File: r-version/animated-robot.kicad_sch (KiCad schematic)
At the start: 81 parts, among them J1 USB_C_Receptacle_USB2.0_16P, J2 Conn_02x03_Odd_Even, J3 Conn_01x02, J4 Conn_01x05, Q1 Q_NMOS_GDS, Q2 Q_NMOS_GDS, Q3 Q_NMOS_GDS, Q4 Q_NMOS_GDS, Q5 Q_NMOS_GDS, Q6 Q_NMOS_GDS, U1 LKS32MC034DOFxQx, U3 XL1509-ADJ, Y1 Crystal_GND24_Small

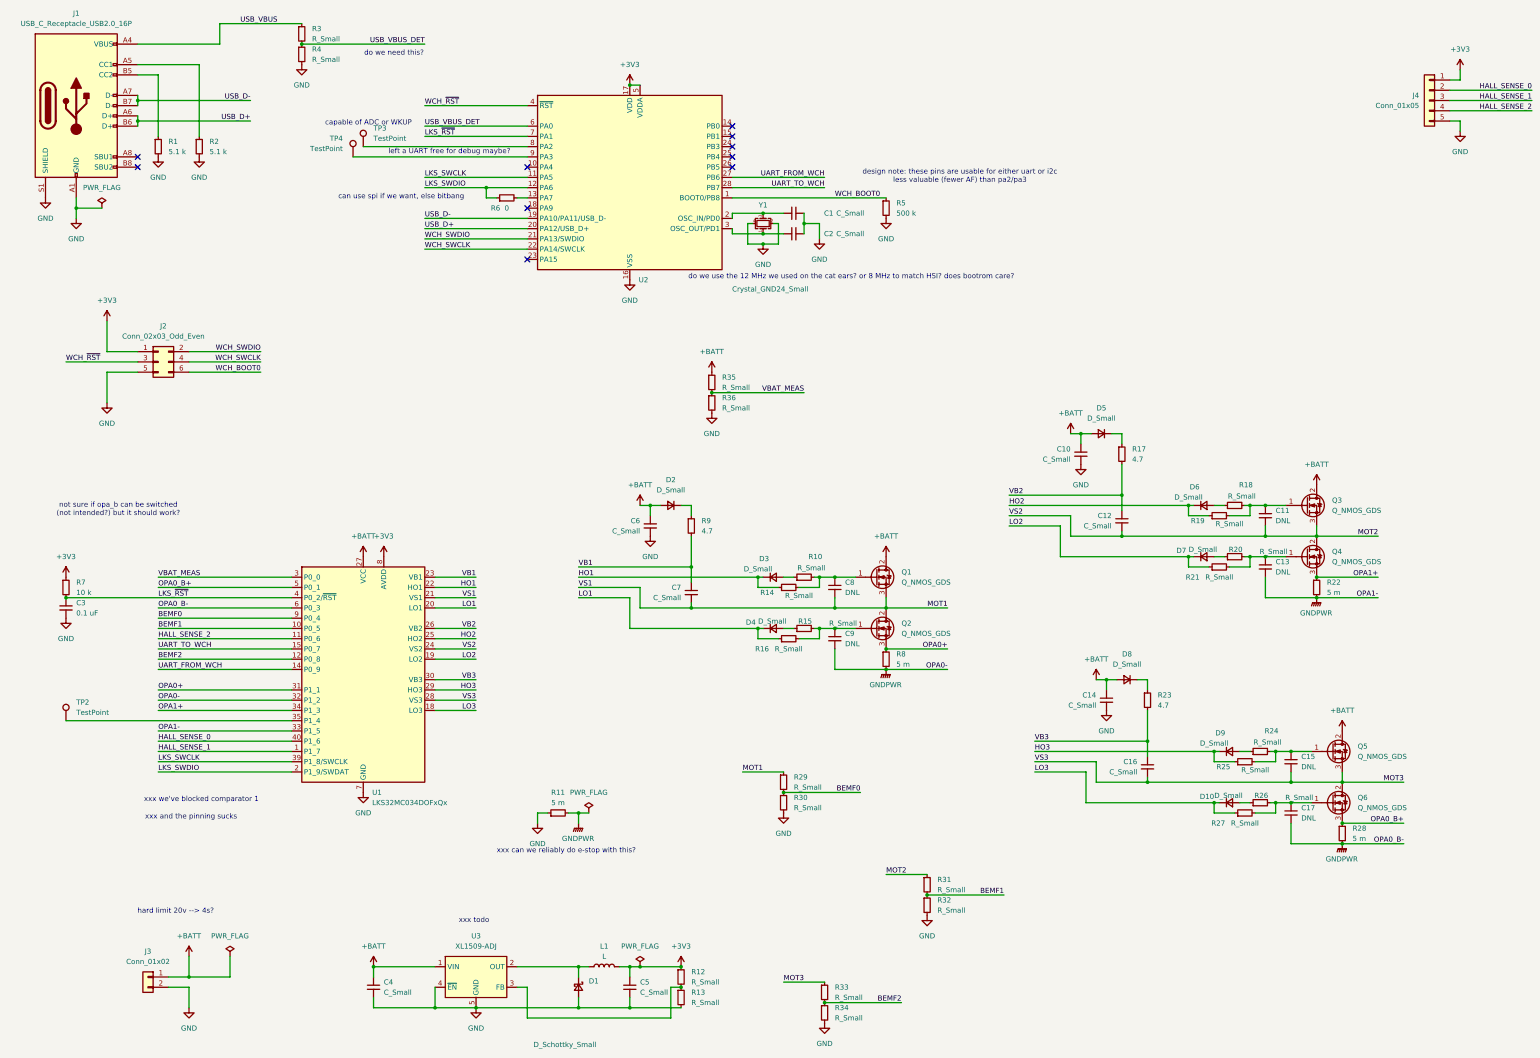
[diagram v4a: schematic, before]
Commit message: fixes to pin assignment
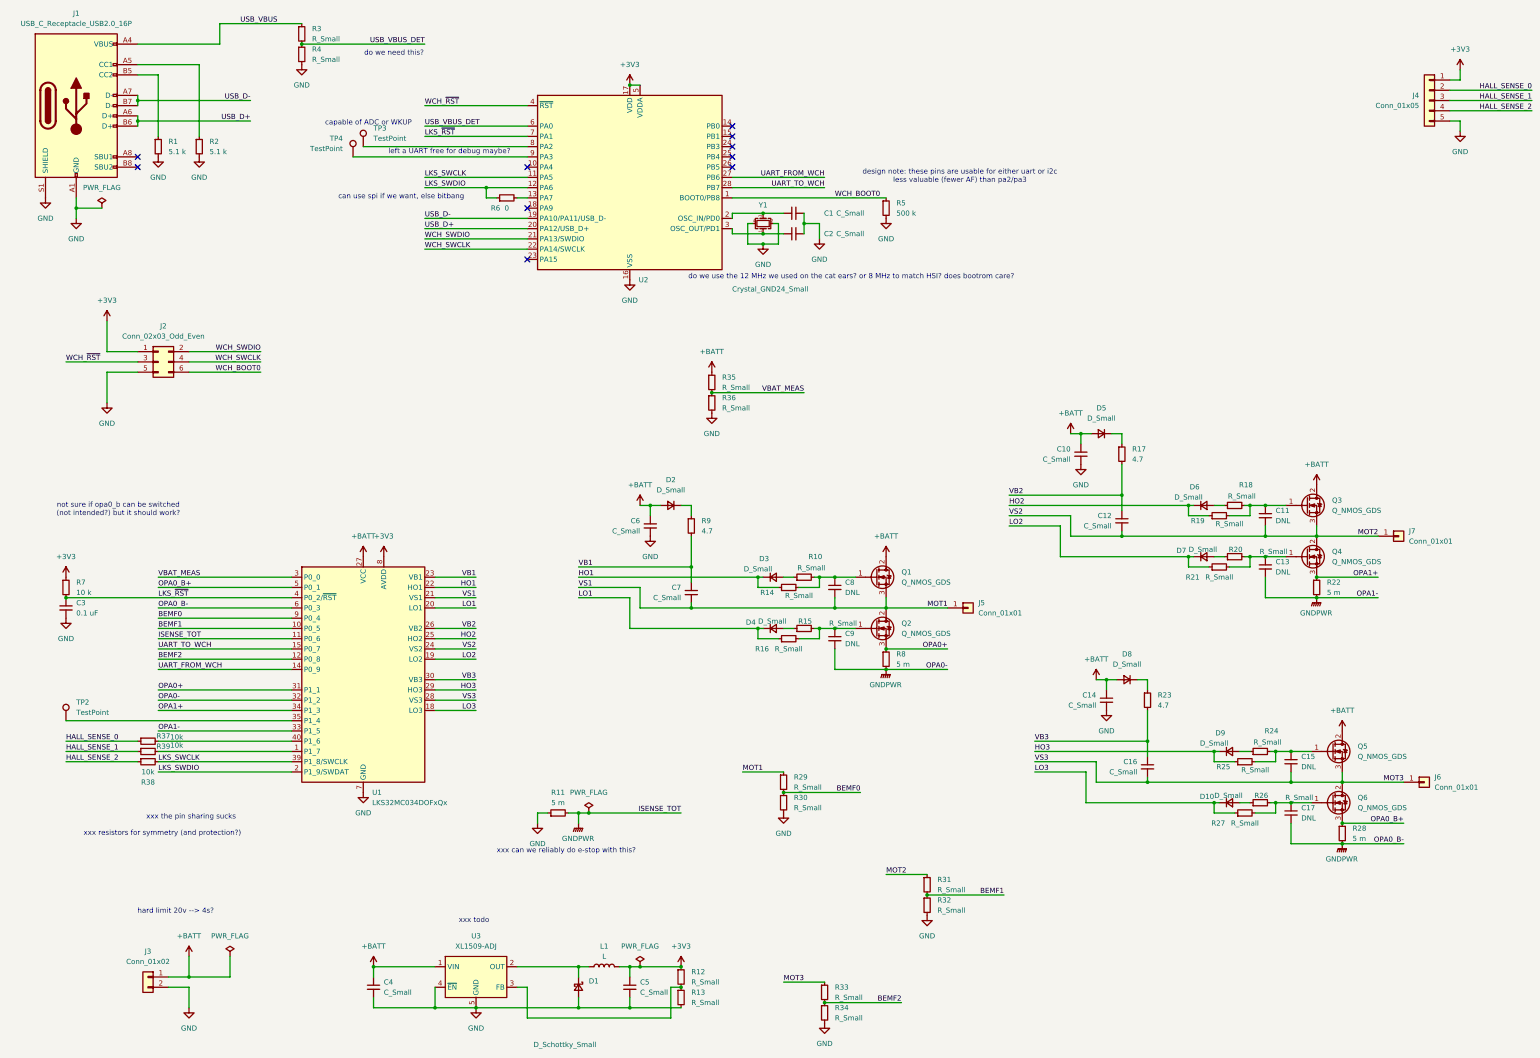
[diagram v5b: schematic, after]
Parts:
- added J5, J6, J7: Conn_01x01, symbol Connector_Generic:Conn_01x01
- added R37, R38, R39: 10k, symbol Device:R_Small
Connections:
- net GNDPWR: now also U1.11 (P0_6)
- net HALL_SENSE_0: now also R37.1; no longer U1.40 (P1_6)
- net HALL_SENSE_1: now also R39.1; no longer U1.1 (P1_7)
- net HALL_SENSE_2: now also R38.1; no longer U1.11 (P0_6)
- net LKS_SWCLK: now also R38.2
- net MOT1: now also J5.1 (Pin_1)
- net MOT2: now also J7.1 (Pin_1)
- net MOT3: now also J6.1 (Pin_1)
- new net: R39.2, U1.1 (P1_7)
- new net: R37.2, U1.40 (P1_6)
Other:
- note added: "not sure if opa0_b can be switched (not intended?) but it should work?"
- note added: "xxx resistors for symmetry (and protection?)"
- note added: "xxx the pin sharing sucks"
- note removed: "not sure if opa_b can be switched (not intended?) but it should work?"
- note removed: "xxx and the pinning sucks"
- note removed: "xxx we've blocked comparator 1"

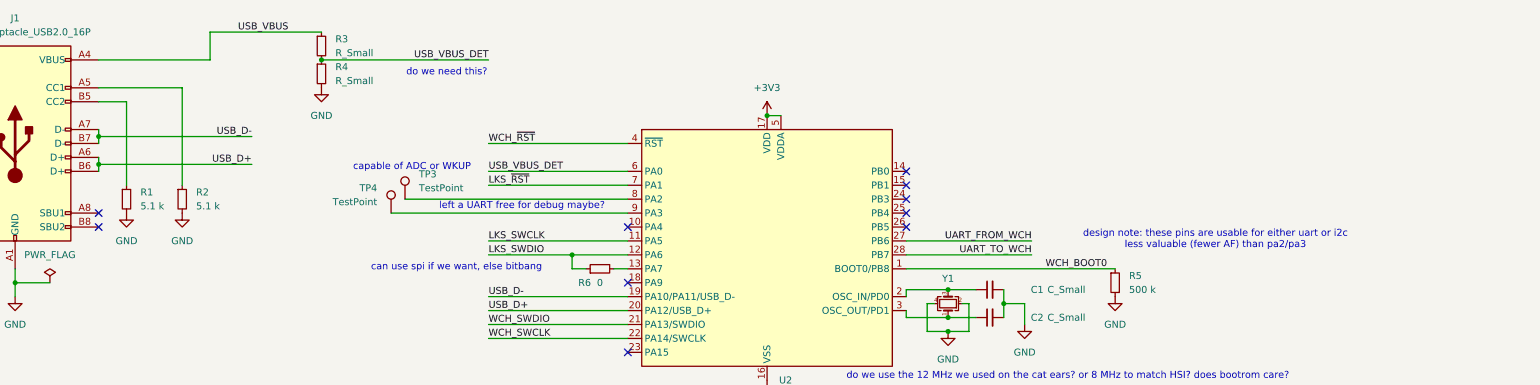
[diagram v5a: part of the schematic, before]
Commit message: fix wch usb vbus det
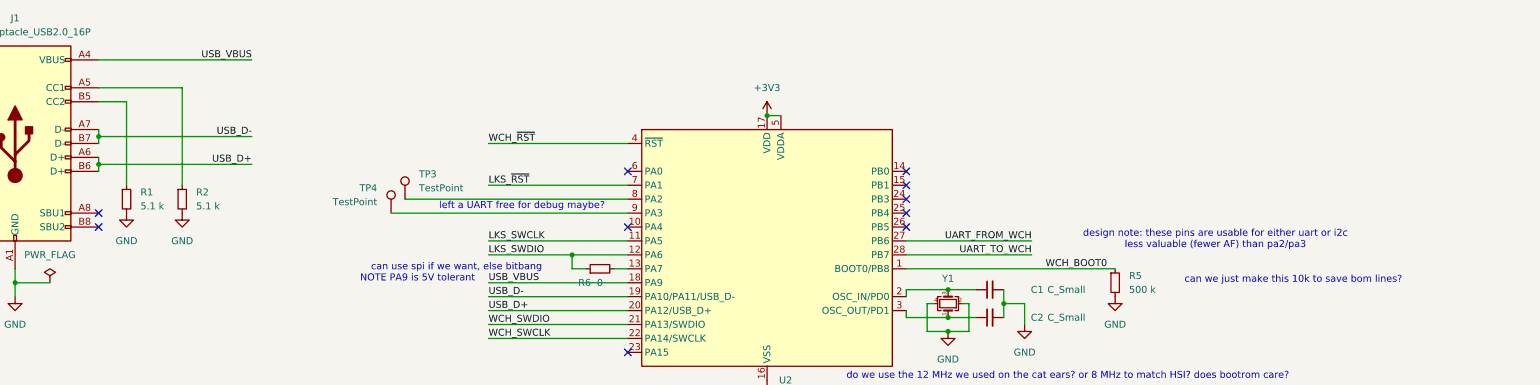
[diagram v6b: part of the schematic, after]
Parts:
- removed R3, R4: R_Small, symbol Device:R_Small
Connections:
- net USB_VBUS: now also U2.18 (PA9)
- net USB_VBUS_DET: no longer names the net of U2.6 (PA0)
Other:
- note added: "NOTE PA9 is 5V tolerant"
- note added: "can we just make this 10k to save bom lines?"
- note removed: "capable of ADC or WKUP"
- note removed: "do we need this?"

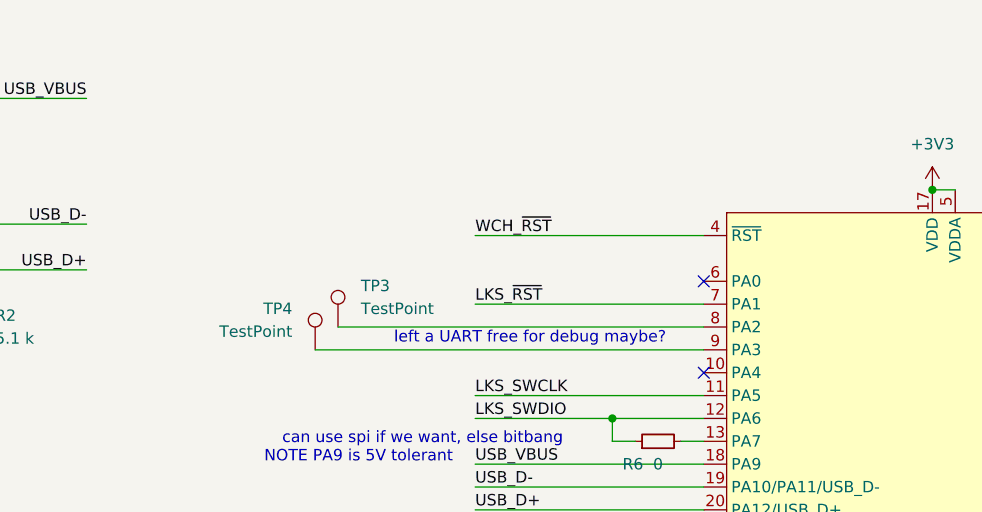
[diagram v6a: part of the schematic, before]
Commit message: add capacitor on wch reset
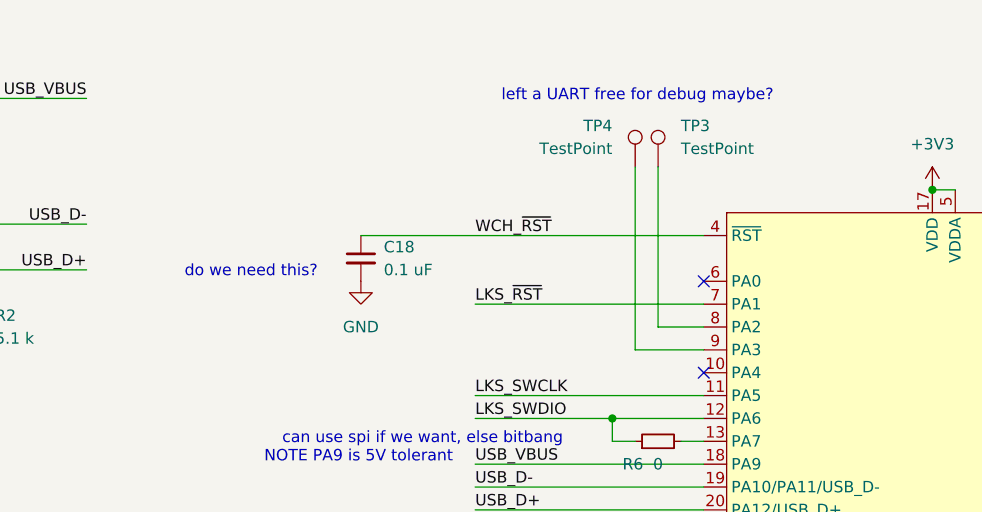
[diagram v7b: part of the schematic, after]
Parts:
- added C18: 0.1 uF, symbol Device:C_Small
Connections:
- net GND: now also C18.2
- net WCH_~{RST}: now also C18.1
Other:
- note added: "do we need this?"
- moved on the sheet: TP3, TP4
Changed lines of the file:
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@@
 	(wire
 		(pts
-			(xy 96.52 50.8) (xy 139.7 50.8)
-		)
-		(stroke
-			(width 0)
-			(type default)
-		)
-	)
-	(wire
-		(pts
 			(xy 180.34 162.56) (xy 215.9 162.56)
 		)
@@
 	(wire
 		(pts
+			(xy 132.08 30.48) (xy 132.08 50.8)
+		)
+		(stroke
+			(width 0)
+			(type default)
+		)
+	)
+	(wire
+		(pts
 			(xy 25.4 160.02) (xy 81.28 160.02)
 		)
@@
 	(wire
 		(pts
-			(xy 114.3 38.1) (xy 139.7 38.1)
-		)
-		(stroke
-			(width 0)
-			(type default)
-		)
-	)
-	(wire
-		(pts
 			(xy 325.12 210.82) (xy 328.93 210.82)
 		)
@@
 	(wire
 		(pts
-			(xy 99.06 48.26) (xy 139.7 48.26)
-		)
-		(stroke
-			(width 0)
-			(type default)
-		)
-	)
-	(wire
-		(pts
 			(xy 132.08 60.96) (xy 129.54 60.96)
 		)
@@
 	(wire
 		(pts
+			(xy 134.62 48.26) (xy 139.7 48.26)
+		)
+		(stroke
+			(width 0)
+			(type default)
+		)
+	)
+	(wire
+		(pts
 			(xy 322.58 144.78) (xy 335.28 144.78)
 		)
@@
 	(wire
 		(pts
+			(xy 134.62 30.48) (xy 134.62 48.26)
+		)
+		(stroke
+			(width 0)
+			(type default)
+		)
+	)
+	(wire
+		(pts
 			(xy 215.9 154.94) (xy 220.98 154.94)
 		)
@@
 	(wire
 		(pts
+			(xy 132.08 50.8) (xy 139.7 50.8)
+		)
+		(stroke
+			(width 0)
+			(type default)
+		)
+	)
+	(wire
+		(pts
 			(xy 27.94 63.5) (xy 27.94 60.96)
 		)
@@
 	(wire
 		(pts
+			(xy 101.6 38.1) (xy 139.7 38.1)
+		)
+		(stroke
+			(width 0)
+			(type default)
+		)
+	)
+	(wire
+		(pts
 			(xy 207.01 170.18) (xy 212.09 170.18)
 		)
@@
 	(text "left a UART free for debug maybe?"
 		(exclude_from_sim no)
-		(at 120.396 49.53 0)
+		(at 132.334 22.606 0)
 		(effects
 			(font
@@
 		)
 	)
+	(text "do we need this?"
+		(exclude_from_sim no)
+		(at 89.408 42.164 0)
+		(effects
+			(font
+				(size 1.27 1.27)
+			)
+		)
+	)
 	(text "hard limit 20v --> 4s?"
 		(exclude_from_sim no)
@@
 	(symbol
 		(lib_id "Connector:TestPoint")
-		(at 99.06 48.26 0)
+		(at 134.62 30.48 0)
 		(unit 1)
 		(exclude_from_sim no)
@@
 		(fields_autoplaced yes)
 		(property "Reference" "TP3"
-			(at 101.6 43.6879 0)
+			(at 137.16 25.9079 0)
 			(effects
 				(font
@@
 		)
 		(property "Value" "TestPoint"
-			(at 101.6 46.2279 0)
+			(at 137.16 28.4479 0)
 			(effects
 				(font
@@
 		)
 		(property "Footprint" ""
-			(at 104.14 48.26 0)
+			(at 139.7 30.48 0)
 			(effects
 				(font
@@
 		)
 		(property "Datasheet" "~"
-			(at 104.14 48.26 0)
+			(at 139.7 30.48 0)
 			(effects
 				(font
@@
 		)
 		(property "Description" "test point"
-			(at 99.06 48.26 0)
+			(at 134.62 30.48 0)
 			(effects
 				(font
@@
 	(symbol
 		(lib_id "Connector:TestPoint")
-		(at 96.52 50.8 0)
+		(at 132.08 30.48 0)
 		(mirror y)
 		(unit 1)
@@
 		(dnp no)
 		(property "Reference" "TP4"
-			(at 93.98 46.2279 0)
+			(at 129.54 25.9079 0)
 			(effects
 				(font
@@
 		)
 		(property "Value" "TestPoint"
-			(at 93.98 48.7679 0)
+			(at 129.54 28.4479 0)
 			(effects
 				(font
@@
 		)
 		(property "Footprint" ""
-			(at 91.44 50.8 0)
+			(at 127 30.48 0)
 			(effects
 				(font
@@
 		)
 		(property "Datasheet" "~"
-			(at 91.44 50.8 0)
+			(at 127 30.48 0)
 			(effects
 				(font
@@
 		)
 		(property "Description" "test point"
-			(at 96.52 50.8 0)
+			(at 132.08 30.48 0)
 			(effects
 				(font
@@
 	)
 	(symbol
+		(lib_id "power:GND")
+		(at 101.6 43.18 0)
+		(unit 1)
+		(exclude_from_sim no)
+		(in_bom yes)
+		(on_board yes)
+		(dnp no)
+		(fields_autoplaced yes)
+		(property "Reference" "#PWR05"
+			(at 101.6 49.53 0)
+			(effects
+				(font
+					(size 1.27 1.27)
+				)
+				(hide yes)
+			)
+		)
+		(property "Value" "GND"
+			(at 101.6 48.26 0)
+			(effects
+				(font
+					(size 1.27 1.27)
+				)
+			)
+		)
+		(property "Footprint" ""
+			(at 101.6 43.18 0)
+			(effects
+				(font
+					(size 1.27 1.27)
+				)
+				(hide yes)
+			)
+		)
+		(property "Datasheet" ""
+			(at 101.6 43.18 0)
+			(effects
+				(font
+					(size 1.27 1.27)
+				)
+				(hide yes)
+			)
+		)
+		(property "Description" "Power symbol creates a global label with name \"GND\" , ground"
+			(at 101.6 43.18 0)
+			(effects
+				(font
+					(size 1.27 1.27)
+				)
+				(hide yes)
+			)
+		)
+		(pin "1"
+		)
+		(instances
+			(project "animated-robot"
+				(path "/8ca1d24f-691f-408a-ac85-5b754cca902e"
+					(reference "#PWR05")
+					(unit 1)
+				)
+			)
+		)
+	)
+	(symbol
 		(lib_id "power:GNDPWR")
 		(at 152.4 215.9 0)
@@
 					(unit 1)
 				)
+			)
+		)
+	)
+	(symbol
+		(lib_id "Device:C_Small")
+		(at 101.6 40.64 0)
+		(unit 1)
+		(exclude_from_sim no)
+		(in_bom yes)
+		(on_board yes)
+		(dnp no)
+		(fields_autoplaced yes)
+		(property "Reference" "C18"
+			(at 104.14 39.3762 0)
+			(effects
+				(font
+					(size 1.27 1.27)
+				)
+				(justify left)
+			)
+		)
+		(property "Value" "0.1 uF"
+			(at 104.14 41.9162 0)
+			(effects
+				(font
+					(size 1.27 1.27)
+				)
+				(justify left)
+			)
+		)
+		(property "Footprint" ""
+			(at 101.6 40.64 0)
+			(effects
+				(font
+					(size 1.27 1.27)
+				)
+				(hide yes)
+			)
+		)
+		(property "Datasheet" "~"
+			(at 101.6 40.64 0)
+			(effects
+				(font
+					(size 1.27 1.27)
+				)
+				(hide yes)
+			)
+		)
+		(property "Description" "Unpolarized capacitor, small symbol"
+			(at 101.6 40.64 0)
+			(effects
+				(font
+					(size 1.27 1.27)
+				)
+				(hide yes)
+			)
+		)
+		(pin "1"
+		)
+		(pin "2"
+		)
+		(instances
+			(project "animated-robot"
+				(path "/8ca1d24f-691f-408a-ac85-5b754cca902e"
+					(reference "C18")
+					(unit 1)
+				)

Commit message: buck converter, after much frustration
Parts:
- C4: value C_Small -> 4.7 uF; LCSC (none) -> C29823
- C5: value C_Small -> 4.7 uF; LCSC (none) -> C1779
- D1: value D_Schottky_Small -> SS34; LCSC (none) -> C8678
- L1: value L -> 47 uH; LCSC (none) -> C497831
- R12: value R_Small -> 33k
- R13: value R_Small -> 20k
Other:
- note added: "47 uH with expected load of no more than 50 mA --> well into DCM xxx how do we calculate proper delta I_L for DCM? forgor with the usual CCM calculations get < ~600 mA and a minimum output cap of 1.6 uF other shrinking is an *optimization*?"
- note added: "cost optimize for jlc output = 3.26 V"
- note added: "recommended lower limit 8v --> min 3s hard limit 20v --> 4s?"
- note added: "xxx this doesn't have a ripple current rating?"
- note removed: "hard limit 20v --> 4s?"
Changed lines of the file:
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@@
 		)
 	)
-	(text "hard limit 20v --> 4s?"
+	(text "47 uH with expected load of no more than 50 mA\n--> well into DCM\n\nxxx how do we calculate proper delta I_L for DCM? forgor\nwith the usual CCM calculations get < ~600 mA\nand a minimum output cap of 1.6 uF\n\nother shrinking is an *optimization*?"
+		(exclude_from_sim no)
+		(at 160.782 234.188 0)
+		(effects
+			(font
+				(size 1.27 1.27)
+			)
+		)
+	)
+	(text "recommended lower limit 8v --> min 3s\nhard limit 20v --> 4s?"
 		(exclude_from_sim no)
 		(at 52.578 237.744 0)
@@
 		)
 	)
+	(text "xxx this doesn't have a ripple current rating?"
+		(exclude_from_sim no)
+		(at 100.33 265.43 0)
+		(effects
+			(font
+				(size 1.27 1.27)
+			)
+		)
+	)
+	(text "cost optimize for jlc\noutput = 3.26 V"
+		(exclude_from_sim no)
+		(at 186.69 265.684 0)
+		(effects
+			(font
+				(size 1.27 1.27)
+			)
+		)
+	)
 	(text "xxx the pin sharing sucks"
 		(exclude_from_sim no)
@@
 			)
 		)
-		(property "Value" "C_Small"
+		(property "Value" "4.7 uF"
 			(at 167.64 257.8162 0)
 			(effects
@@
 			)
 		)
+		(property "LCSC" "C1779"
+			(at 165.1 256.54 0)
+			(effects
+				(font
+					(size 1.27 1.27)
+				)
+				(hide yes)
+			)
+		)
 		(pin "2"
 		)
@@
 			)
 		)
-		(property "Value" "C_Small"
+		(property "Value" "4.7 uF"
 			(at 104.14 257.8162 0)
 			(effects
@@
 			)
 		)
+		(property "LCSC" "C29823"
+			(at 101.6 256.54 0)
+			(effects
+				(font
+					(size 1.27 1.27)
+				)
+				(hide yes)
+			)
+		)
 		(pin "2"
 		)
@@
 			)
 		)
-		(property "Value" "R_Small"
+		(property "Value" "20k"
 			(at 180.34 260.3499 0)
 			(effects
@@
 			)
 		)
-		(property "Value" "D_Schottky_Small"
-			(at 141.224 270.764 90)
+		(property "Value" "SS34"
+			(at 155.702 258.064 90)
 			(effects
 				(font
@@
 			)
 		)
+		(property "LCSC" "C8678"
+			(at 152.4 256.54 90)
+			(effects
+				(font
+					(size 1.27 1.27)
+				)
+				(hide yes)
+			)
+		)
 		(pin "1"
 		)
@@
 			)
 		)
-		(property "Value" "R_Small"
+		(property "Value" "33k"
 			(at 180.34 255.2699 0)
 			(effects
@@
 			)
 		)
-		(property "Value" "L"
+		(property "Value" "47 uH"
 			(at 158.75 248.92 90)
 			(effects
@@
 			(effects
 				(font
+					(size 1.27 1.27)
+				)
+				(hide yes)
+			)
+		)
+		(property "LCSC" "C497831"
+			(at 158.75 251.46 90)
+			(effects
+				(font
